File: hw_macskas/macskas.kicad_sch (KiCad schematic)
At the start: 39 parts, among them J1 Conn_2Rows-05Pins, Q1 AO3401A, Q2 AO3401A, Q3 AO3401A, SW1 SW_DPST_x2, T1 Tab, U1 PY32F002AF15P6TU

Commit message: Working on cat design.
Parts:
- removed D1: LED_ARGB, karifa:LED_RGB_Wuerth-PLCC4_3.2x2.8mm_150141M173100, symbol Device:LED_ARGB
- removed R10, R11: 100k, Resistor_SMD:R_0603_1608Metric, symbol Device:R
- added D13, D14, D15, D16, D17, D18: LED, LED_SMD:LED_0805_2012Metric, symbol Device:LED
- added T2, T3, T4, T5, T6: Tab, kikit:Tab, symbol kikit:Tab
- BT1: value Battery -> CR2032
- L1, L2, L3: value L -> 1mH; footprint Inductor_SMD:L_1008_2520Metric -> Inductor_SMD:L_Ferrocore_DLG-0403
- R2: renamed from R4; value 1k -> 10
- R3: renamed from R5; value 1k -> 10
- R4: renamed from R6; value 1k -> 10
- R5: renamed from R7; value 1k -> 10
- R6: renamed from R8; value 1k -> 10
- R7: renamed from R9; value 1k -> 10
- renumbered C2 to C1, C3 to C2, C1 to C3, D2 to D1, D9 to D10, D13 to D12, D4 to D2, D6 to D3, D8 to D4, D10 to D5, D12 to D6, D3 to D7, D5 to D8, D7 to D9, R3 to R10, R2 to R8, R12 to R9
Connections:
- net B is gone; now on net MPX1: Q1.1 (G), R1.2, U1.12 (PA1)
- net R is gone; now on net MPX2: Q2.1 (G), R8.2, U1.11 (PA0)
- net GND: no longer L1.2, L2.2
- net MPX1: now also L1.2; no longer D10.1 (K), D11.1 (K), D12.1 (K), D7.1 (K), D8.1 (K), D9.1 (K), U1.6 (PA6)
- net MPX2: now also L2.2; no longer D1.1 (K), D2.1 (K), D3.1 (K), D4.1 (K), D5.1 (K), D6.1 (K), U1.7 (PA5)
- net at D11.2 (A), D5.2 (A), R6.1: now also D17.2 (A)
- net at D12.2 (A), D6.2 (A), R7.1: now also D18.2 (A)
- net at L2.1, Q2.3 (D): now also D10.1 (K), D11.1 (K), D12.1 (K), D7.1 (K), D8.1 (K), D9.1 (K)
- net at D3.2 (A), D9.2 (A), R4.1: now also D15.2 (A)
- net at L3.1, Q3.3 (D): now also D13.1 (K), D14.1 (K), D15.1 (K), D16.1 (K), D17.1 (K), D18.1 (K)
- net at D1.2 (A), D7.2 (A), R2.1: now also D13.2 (A)
- net at D2.2 (A), D8.2 (A), R3.1: now also D14.2 (A)
- net at D10.2 (A), D4.2 (A), R5.1: now also D16.2 (A)
- net at L1.1, Q1.3 (D): now also D1.1 (K), D2.1 (K), D3.1 (K), D4.1 (K), D5.1 (K), D6.1 (K)
- net G renamed MPX3
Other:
- moved on the sheet: BT1, C1, C2, C3, D1, D10, D11, D12, D2, D3, D4, D5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

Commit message: Updated cat.
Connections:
- net GND: no longer L3.2
- net MPX3: now also L3.2
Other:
- moved on the sheet: L3
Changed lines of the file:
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@@
 	(wire
 		(pts
-			(xy 149.86 101.6) (xy 149.86 104.14)
-		)
-		(stroke
-			(width 0)
-			(type default)
-		)
-	)
-	(wire
-		(pts
 			(xy 127 109.22) (xy 140.97 109.22)
 		)
@@
 	(wire
 		(pts
-			(xy 140.97 109.22) (xy 140.97 116.84)
-		)
-		(stroke
-			(width 0)
-			(type default)
-		)
-	)
-	(wire
-		(pts
 			(xy 269.24 99.06) (xy 269.24 101.6)
 		)
@@
 	(wire
 		(pts
+			(xy 140.97 109.22) (xy 149.86 109.22)
+		)
+		(stroke
+			(width 0)
+			(type default)
+		)
+	)
+	(wire
+		(pts
 			(xy 193.04 69.85) (xy 212.09 69.85)
 		)
@@
 	(wire
 		(pts
+			(xy 140.97 109.22) (xy 140.97 116.84)
+		)
+		(stroke
+			(width 0)
+			(type default)
+		)
+	)
+	(wire
+		(pts
 			(xy 193.04 91.44) (xy 193.04 82.55)
 		)
@@
 	(symbol
 		(lib_id "Device:L")
-		(at 149.86 107.95 0)
+		(at 149.86 105.41 0)
 		(unit 1)
 		(exclude_from_sim no)
@@
 		(fields_autoplaced yes)
 		(property "Reference" "L3"
-			(at 151.13 106.6799 0)
+			(at 151.13 104.1399 0)
 			(effects
 				(font
@@
 		)
 		(property "Value" "1mH"
-			(at 151.13 109.2199 0)
+			(at 151.13 106.6799 0)
 			(effects
 				(font
@@
 		)
 		(property "Footprint" "Inductor_SMD:L_Ferrocore_DLG-0403"
-			(at 149.86 107.95 0)
+			(at 149.86 105.41 0)
 			(effects
 				(font
@@
 		)
 		(property "Datasheet" "~"
-			(at 149.86 107.95 0)
+			(at 149.86 105.41 0)
 			(effects
 				(font
@@
 		)
 		(property "Description" ""
-			(at 149.86 107.95 0)
+			(at 149.86 105.41 0)
 			(effects
 				(font
@@
 					(unit 1)
 				)
-			)
-		)
-	)
-	(symbol
-		(lib_id "power:GND")
-		(at 149.86 111.76 0)
-		(unit 1)
-		(exclude_from_sim no)
-		(in_bom yes)
-		(on_board yes)
-		(dnp no)
-		(fields_autoplaced yes)
-		(property "Reference" "#PWR016"
-			(at 149.86 118.11 0)
-			(effects
-				(font
-					(size 1.27 1.27)
-				)
-				(hide yes)
-			)
-		)
-		(property "Value" "GND"
-			(at 152.4 113.0299 0)
-			(effects
-				(font
-					(size 1.27 1.27)
-				)
-				(justify left)
-			)
-		)
-		(property "Footprint" ""
-			(at 149.86 111.76 0)
-			(effects
-				(font
-					(size 1.27 1.27)
-				)
-				(hide yes)
-			)
-		)
-		(property "Datasheet" ""
-			(at 149.86 111.76 0)
-			(effects
-				(font
-					(size 1.27 1.27)
-				)
-				(hide yes)
-			)
-		)
-		(property "Description" ""
-			(at 149.86 111.76 0)
-			(effects
-				(font
-					(size 1.27 1.27)
-				)
-				(hide yes)
-			)
-		)
-		(pin "1"
-		)
-		(instances
-			(project "hopehely"
-				(path "/30f28fd8-ef05-4208-b612-7ffefcdba2ba"
-					(reference "#PWR016")
-					(unit 1)
-				)

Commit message: Panelized.
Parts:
- removed T4, T5, T6: Tab, kikit:Tab, symbol kikit:Tab
- T1, T2, T3: footprint kikit:Tab -> PCM_kikit:Tab
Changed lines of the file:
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@@
 			)
 		)
-		(property "Footprint" "kikit:Tab"
+		(property "Footprint" "PCM_kikit:Tab"
 			(at 25.4 185.42 0)
 			(effects
@@
 			)
 		)
-		(property "Footprint" "kikit:Tab"
+		(property "Footprint" "PCM_kikit:Tab"
 			(at 53.34 185.42 0)
 			(effects
@@
 	)
 	(symbol
-		(lib_id "kikit:Tab")
-		(at 95.25 185.42 0)
-		(unit 1)
-		(exclude_from_sim no)
-		(in_bom no)
-		(on_board yes)
-		(dnp no)
-		(fields_autoplaced yes)
-		(property "Reference" "T6"
-			(at 100.33 183.5149 0)
-			(effects
-				(font
-					(size 1.27 1.27)
-				)
-				(justify left)
-			)
-		)
-		(property "Value" "Tab"
-			(at 100.33 186.0549 0)
-			(effects
-				(font
-					(size 1.27 1.27)
-				)
-				(justify left)
-			)
-		)
-		(property "Footprint" "kikit:Tab"
-			(at 95.25 185.42 0)
-			(effects
-				(font
-					(size 1.27 1.27)
-				)
-				(hide yes)
-			)
-		)
-		(property "Datasheet" ""
-			(at 95.25 185.42 0)
-			(effects
-				(font
-					(size 1.27 1.27)
-				)
-				(hide yes)
-			)
-		)
-		(property "Description" ""
-			(at 95.25 185.42 0)
-			(effects
-				(font
-					(size 1.27 1.27)
-				)
-				(hide yes)
-			)
-		)
-		(instances
-			(project "macskas"
-				(path "/30f28fd8-ef05-4208-b612-7ffefcdba2ba"
-					(reference "T6")
-					(unit 1)
-				)
-			)
-		)
-	)
-	(symbol
 		(lib_id "Device:LED")
 		(at 193.04 45.72 270)
@@
 			)
 		)
-		(property "Footprint" "kikit:Tab"
+		(property "Footprint" "PCM_kikit:Tab"
 			(at 39.37 185.42 0)
 			(effects
@@
 	)
 	(symbol
-		(lib_id "kikit:Tab")
-		(at 67.31 185.42 0)
-		(unit 1)
-		(exclude_from_sim no)
-		(in_bom no)
-		(on_board yes)
-		(dnp no)
-		(fields_autoplaced yes)
-		(property "Reference" "T4"
-			(at 72.39 183.5149 0)
-			(effects
-				(font
-					(size 1.27 1.27)
-				)
-				(justify left)
-			)
-		)
-		(property "Value" "Tab"
-			(at 72.39 186.0549 0)
-			(effects
-				(font
-					(size 1.27 1.27)
-				)
-				(justify left)
-			)
-		)
-		(property "Footprint" "kikit:Tab"
-			(at 67.31 185.42 0)
-			(effects
-				(font
-					(size 1.27 1.27)
-				)
-				(hide yes)
-			)
-		)
-		(property "Datasheet" ""
-			(at 67.31 185.42 0)
-			(effects
-				(font
-					(size 1.27 1.27)
-				)
-				(hide yes)
-			)
-		)
-		(property "Description" ""
-			(at 67.31 185.42 0)
-			(effects
-				(font
-					(size 1.27 1.27)
-				)
-				(hide yes)
-			)
-		)
-		(instances
-			(project "macskas"
-				(path "/30f28fd8-ef05-4208-b612-7ffefcdba2ba"
-					(reference "T4")
-					(unit 1)
-				)
-			)
-		)
-	)
-	(symbol
 		(lib_id "Device:R")
 		(at 240.03 54.61 270)
@@
 					(unit 1)
 				)
-			)
-		)
-	)
-	(symbol
-		(lib_id "kikit:Tab")
-		(at 81.28 185.42 0)
-		(unit 1)
-		(exclude_from_sim no)
-		(in_bom no)
-		(on_board yes)
-		(dnp no)
-		(fields_autoplaced yes)
-		(property "Reference" "T5"
-			(at 86.36 183.5149 0)
-			(effects
-				(font
-					(size 1.27 1.27)
-				)
-				(justify left)
-			)
-		)
-		(property "Value" "Tab"
-			(at 86.36 186.0549 0)
-			(effects
-				(font
-					(size 1.27 1.27)
-				)
-				(justify left)
-			)
-		)
-		(property "Footprint" "kikit:Tab"
-			(at 81.28 185.42 0)
-			(effects
-				(font
-					(size 1.27 1.27)
-				)
-				(hide yes)
-			)
-		)
-		(property "Datasheet" ""
-			(at 81.28 185.42 0)
-			(effects
-				(font
-					(size 1.27 1.27)
-				)
-				(hide yes)
-			)
-		)
-		(property "Description" ""
-			(at 81.28 185.42 0)
-			(effects
-				(font
-					(size 1.27 1.27)
-				)
-				(hide yes)
-			)
-		)
-		(instances
-			(project "macskas"
-				(path "/30f28fd8-ef05-4208-b612-7ffefcdba2ba"
-					(reference "T5")
-					(unit 1)
-				)

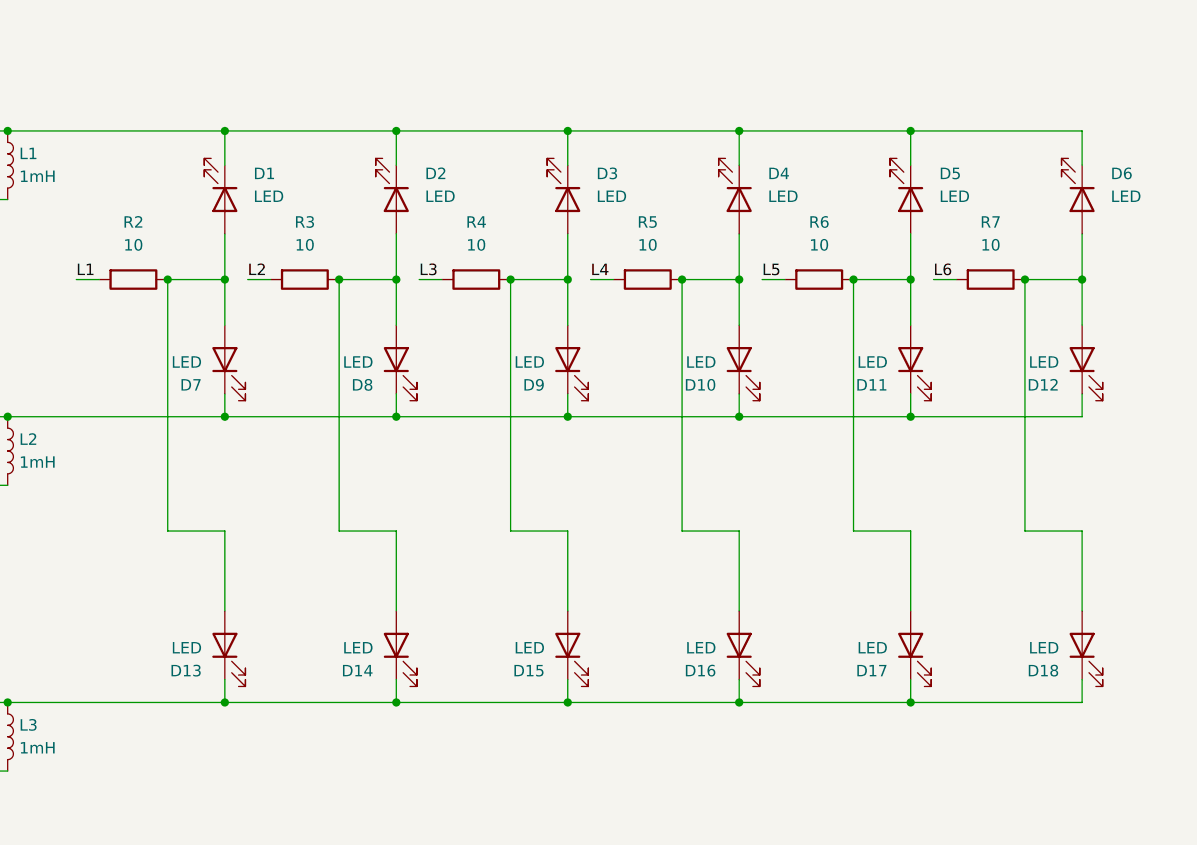
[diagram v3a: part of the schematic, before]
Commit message: Soldering guide.
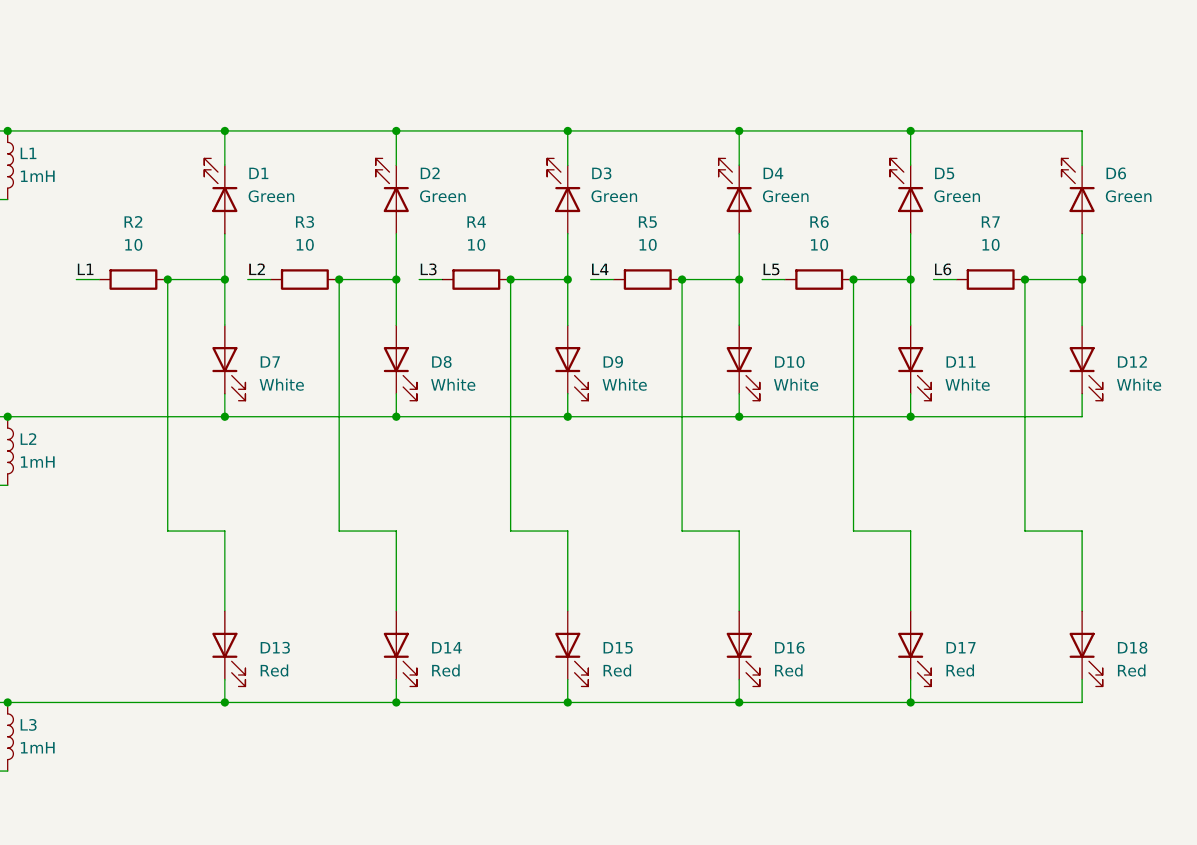
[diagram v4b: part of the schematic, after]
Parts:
- D1, D2, D3, D4, D5, D6: value LED -> Green
- D10, D11, D12, D7, D8, D9: value LED -> White
- D13, D14, D15, D16, D17, D18: value LED -> Red
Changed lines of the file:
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@@
 		(fields_autoplaced yes)
 		(property "Reference" "D11"
-			(at 247.65 66.3576 90)
+			(at 254 63.8174 90)
 			(effects
 				(font
 					(size 1.27 1.27)
 				)
-				(justify left)
+				(justify right)
 			)
 		)
-		(property "Value" "LED"
-			(at 247.65 63.8176 90)
+		(property "Value" "White"
+			(at 254 66.3574 90)
 			(effects
 				(font
 					(size 1.27 1.27)
 				)
-				(justify left)
+				(justify right)
 			)
 		)
@@
 		(fields_autoplaced yes)
 		(property "Reference" "D3"
-			(at 215.265 42.8624 90)
+			(at 214.63 42.8624 90)
 			(effects
 				(font
@@
 			)
 		)
-		(property "Value" "LED"
-			(at 215.265 45.4024 90)
+		(property "Value" "Green"
+			(at 214.63 45.4024 90)
 			(effects
 				(font
@@
 		(fields_autoplaced yes)
 		(property "Reference" "D18"
-			(at 266.7 98.1076 90)
+			(at 273.05 95.5674 90)
 			(effects
 				(font
 					(size 1.27 1.27)
 				)
-				(justify left)
+				(justify right)
 			)
 		)
-		(property "Value" "LED"
-			(at 266.7 95.5676 90)
+		(property "Value" "Red"
+			(at 273.05 98.1074 90)
 			(effects
 				(font
 					(size 1.27 1.27)
 				)
-				(justify left)
+				(justify right)
 			)
 		)
@@
 		(fields_autoplaced yes)
 		(property "Reference" "D1"
-			(at 177.165 42.8624 90)
+			(at 176.53 42.8624 90)
 			(effects
 				(font
@@
 			)
 		)
-		(property "Value" "LED"
-			(at 177.165 45.4024 90)
+		(property "Value" "Green"
+			(at 176.53 45.4024 90)
 			(effects
 				(font
@@
 		(fields_autoplaced yes)
 		(property "Reference" "D2"
-			(at 196.215 42.8624 90)
+			(at 195.58 42.8624 90)
 			(effects
 				(font
@@
 			)
 		)
-		(property "Value" "LED"
-			(at 196.215 45.4024 90)
+		(property "Value" "Green"
+			(at 195.58 45.4024 90)
 			(effects
 				(font
@@
 		(fields_autoplaced yes)
 		(property "Reference" "D14"
-			(at 190.5 98.1076 90)
+			(at 196.85 95.5674 90)
 			(effects
 				(font
 					(size 1.27 1.27)
 				)
-				(justify left)
+				(justify right)
 			)
 		)
-		(property "Value" "LED"
-			(at 190.5 95.5676 90)
+		(property "Value" "Red"
+			(at 196.85 98.1074 90)
 			(effects
 				(font
 					(size 1.27 1.27)
 				)
-				(justify left)
+				(justify right)
 			)
 		)
@@
 		(fields_autoplaced yes)
 		(property "Reference" "D16"
-			(at 228.6 98.1076 90)
+			(at 234.95 95.5674 90)
 			(effects
 				(font
 					(size 1.27 1.27)
 				)
-				(justify left)
+				(justify right)
 			)
 		)
-		(property "Value" "LED"
-			(at 228.6 95.5676 90)
+		(property "Value" "Red"
+			(at 234.95 98.1074 90)
 			(effects
 				(font
 					(size 1.27 1.27)
 				)
-				(justify left)
+				(justify right)
 			)
 		)
@@
 		(fields_autoplaced yes)
 		(property "Reference" "D12"
-			(at 266.7 66.3576 90)
+			(at 273.05 63.8174 90)
 			(effects
 				(font
 					(size 1.27 1.27)
 				)
-				(justify left)
+				(justify right)
 			)
 		)
-		(property "Value" "LED"
-			(at 266.7 63.8176 90)
+		(property "Value" "White"
+			(at 273.05 66.3574 90)
 			(effects
 				(font
 					(size 1.27 1.27)
 				)
-				(justify left)
+				(justify right)
 			)
 		)
@@
 		(fields_autoplaced yes)
 		(property "Reference" "D5"
-			(at 253.365 42.8624 90)
+			(at 252.73 42.8624 90)
 			(effects
 				(font
@@
 			)
 		)
-		(property "Value" "LED"
-			(at 253.365 45.4024 90)
+		(property "Value" "Green"
+			(at 252.73 45.4024 90)
 			(effects
 				(font
@@
 		(fields_autoplaced yes)
 		(property "Reference" "D6"
-			(at 272.415 42.8624 90)
+			(at 271.78 42.8624 90)
 			(effects
 				(font
@@
 			)
 		)
-		(property "Value" "LED"
-			(at 272.415 45.4024 90)
+		(property "Value" "Green"
+			(at 271.78 45.4024 90)
 			(effects
 				(font
@@
 		(fields_autoplaced yes)
 		(property "Reference" "D8"
-			(at 190.5 66.3576 90)
+			(at 196.85 63.8174 90)
 			(effects
 				(font
 					(size 1.27 1.27)
 				)
-				(justify left)
+				(justify right)
 			)
 		)
-		(property "Value" "LED"
-			(at 190.5 63.8176 90)
+		(property "Value" "White"
+			(at 196.85 66.3574 90)
 			(effects
 				(font
 					(size 1.27 1.27)
 				)
-				(justify left)
+				(justify right)
 			)
 		)
@@
 		(fields_autoplaced yes)
 		(property "Reference" "D15"
-			(at 209.55 98.1076 90)
+			(at 215.9 95.5674 90)
 			(effects
 				(font
 					(size 1.27 1.27)
 				)
-				(justify left)
+				(justify right)
 			)
 		)
-		(property "Value" "LED"
-			(at 209.55 95.5676 90)
+		(property "Value" "Red"
+			(at 215.9 98.1074 90)
 			(effects
 				(font
 					(size 1.27 1.27)
 				)
-				(justify left)
+				(justify right)
 			)
 		)
@@
 		(fields_autoplaced yes)
 		(property "Reference" "D10"
-			(at 228.6 66.3576 90)
+			(at 234.95 63.8174 90)
 			(effects
 				(font
 					(size 1.27 1.27)
 				)
-				(justify left)
+				(justify right)
 			)
 		)
-		(property "Value" "LED"
-			(at 228.6 63.8176 90)
+		(property "Value" "White"
+			(at 234.95 66.3574 90)
 			(effects
 				(font
 					(size 1.27 1.27)
 				)
-				(justify left)
+				(justify right)
 			)
 		)
@@
 		(fields_autoplaced yes)
 		(property "Reference" "D9"
-			(at 209.55 66.3576 90)
+			(at 215.9 63.8174 90)
 			(effects
 				(font
 					(size 1.27 1.27)
 				)
-				(justify left)
+				(justify right)
 			)
 		)
-		(property "Value" "LED"
-			(at 209.55 63.8176 90)
+		(property "Value" "White"
+			(at 215.9 66.3574 90)
 			(effects
 				(font
 					(size 1.27 1.27)
 				)
-				(justify left)
+				(justify right)
 			)
 		)
@@
 		(fields_autoplaced yes)
 		(property "Reference" "D7"
-			(at 171.45 66.3576 90)
+			(at 177.8 63.8174 90)
 			(effects
 				(font
 					(size 1.27 1.27)
 				)
-				(justify left)
+				(justify right)
 			)
 		)
-		(property "Value" "LED"
-			(at 171.45 63.8176 90)
+		(property "Value" "White"
+			(at 177.8 66.3574 90)
 			(effects
 				(font
 					(size 1.27 1.27)
 				)
-				(justify left)
+				(justify right)
 			)
 		)
@@
 		(fields_autoplaced yes)
 		(property "Reference" "D17"
-			(at 247.65 98.1076 90)
+			(at 254 95.5674 90)
 			(effects
 				(font
 					(size 1.27 1.27)
 				)
-				(justify left)
+				(justify right)
 			)
 		)
-		(property "Value" "LED"
-			(at 247.65 95.5676 90)
+		(property "Value" "Red"
+			(at 254 98.1074 90)
 			(effects
 				(font
 					(size 1.27 1.27)
 				)
-				(justify left)
+				(justify right)
 			)
 		)
@@
 		(fields_autoplaced yes)
 		(property "Reference" "D13"
-			(at 171.45 98.1076 90)
+			(at 177.8 95.5674 90)
 			(effects
 				(font
 					(size 1.27 1.27)
 				)
-				(justify left)
+				(justify right)
 			)
 		)
-		(property "Value" "LED"
-			(at 171.45 95.5676 90)
+		(property "Value" "Red"
+			(at 177.8 98.1074 90)
 			(effects
 				(font
 					(size 1.27 1.27)
 				)
-				(justify left)
+				(justify right)
 			)
 		)
@@
 		(fields_autoplaced yes)
 		(property "Reference" "D4"
-			(at 234.315 42.8624 90)
+			(at 233.68 42.8624 90)
 			(effects
 				(font
@@
 			)
 		)
-		(property "Value" "LED"
-			(at 234.315 45.4024 90)
+		(property "Value" "Green"
+			(at 233.68 45.4024 90)
 			(effects
 				(font
